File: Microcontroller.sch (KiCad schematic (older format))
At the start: 42 parts, among them CN1 2x10_Way_2.54mm_Pitch_Header, CN2 CONN_RCPT_USB2.0_MINI_B_SMD_R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, J3 DB1C-A1LD, J4 DB1C-A1LD, J5 DB1C-A1LD, U2 STM32L412R8T6, X1 ABM3B-16.000MHZ

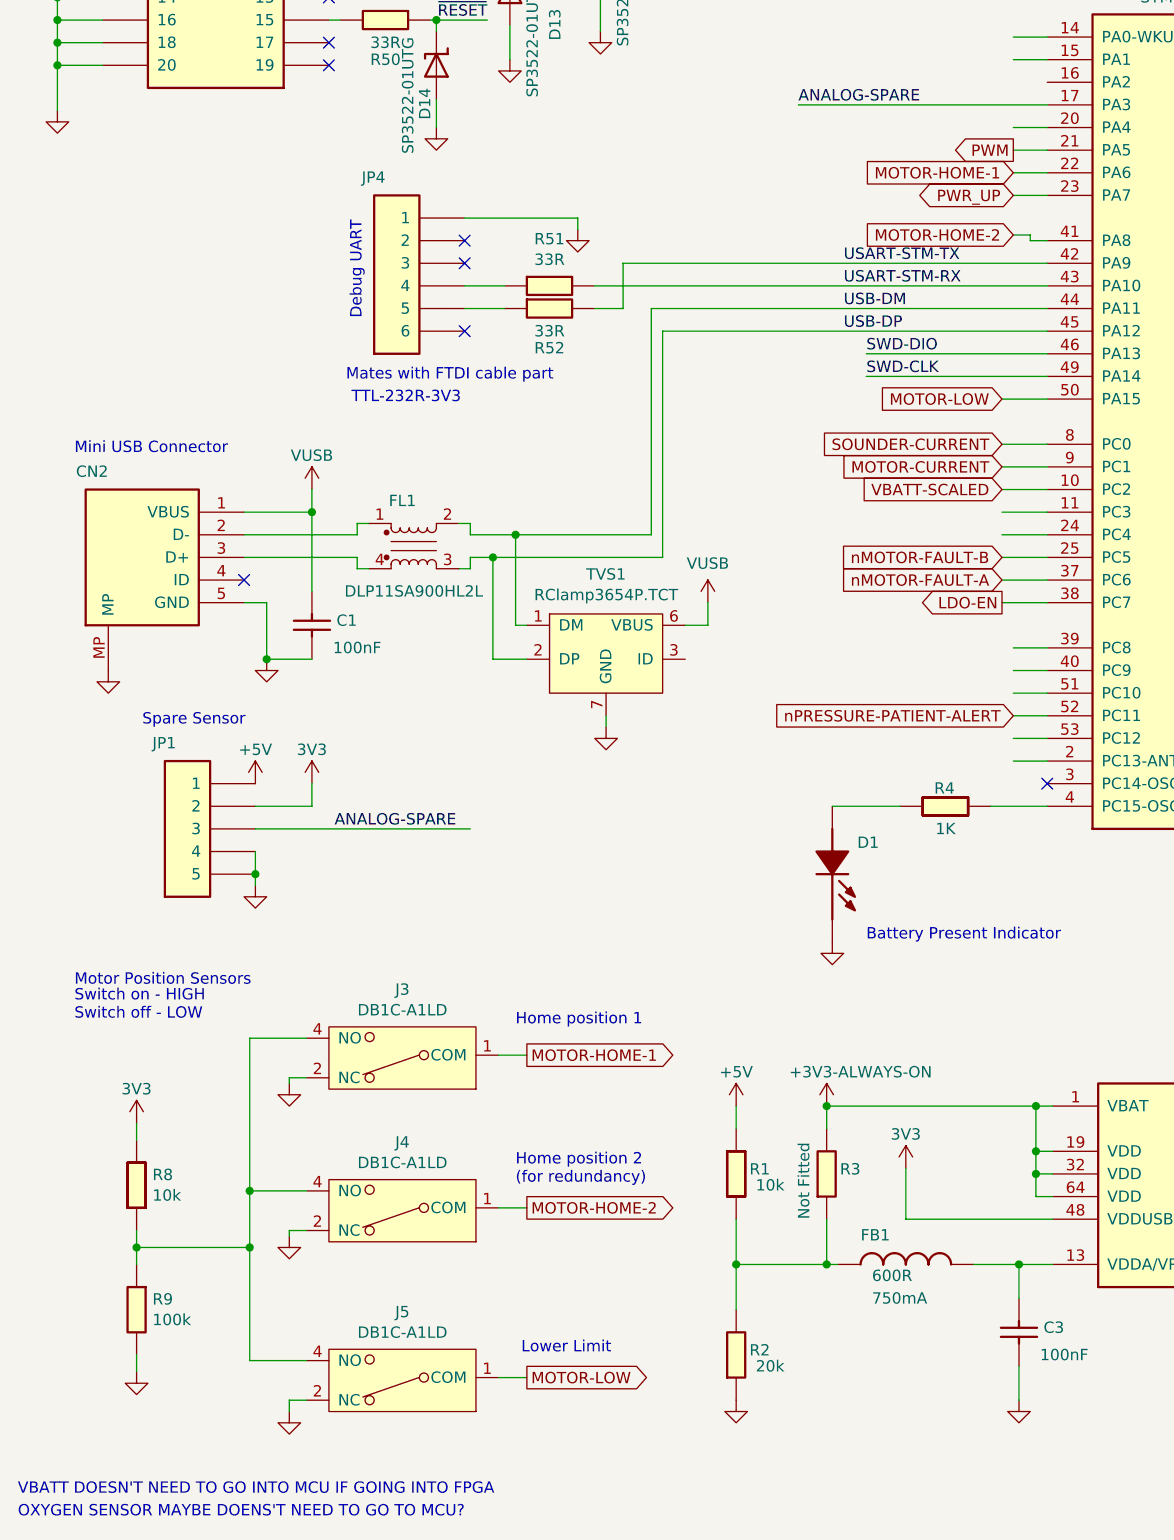
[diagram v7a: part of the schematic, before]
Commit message: On-board Microswitch signals removed from. Microswitch signals from power board renamed to "SW_Home" etc
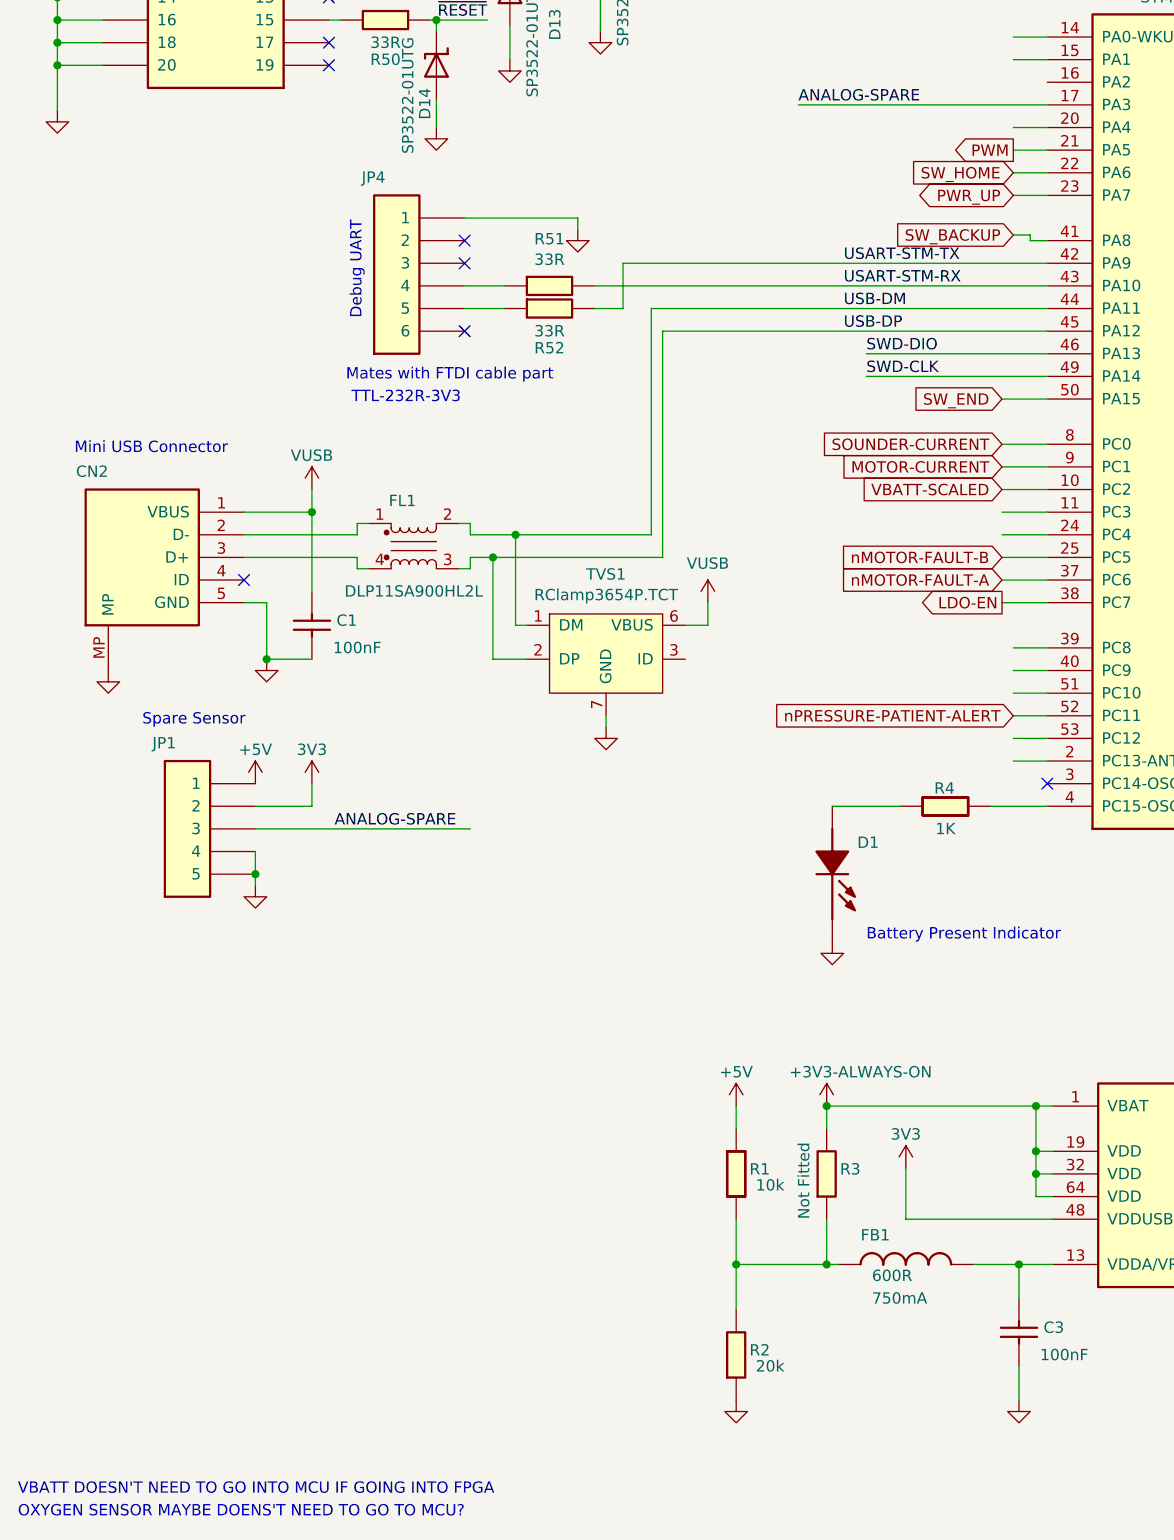
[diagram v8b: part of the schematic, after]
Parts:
- removed J3, J4, J5: DB1C-A1LD, symbol OpenVent-rescue:DB1C-A1LD-OpenVent
- removed R8: 10k_0603_Chip_Resistor,_1%,_0.1W, symbol OpenVent:10k_0603_Chip_Resistor,_1%,_0.1W
- removed R9: 100K_0603_Chip_Resistor,_1%,_0.1W, symbol OpenVent:100K_0603_Chip_Resistor,_1%,_0.1W
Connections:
- net labels added: SW_BACKUP, SW_END, SW_HOME
- net labels removed: MOTOR-HOME-1, MOTOR-HOME-2, MOTOR-LOW
- wire segments 205 -> 185
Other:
- note removed: "Home position 1"
- note removed: "Home position 2\n(for redundancy)"
- note removed: "Lower Limit"
- note removed: "Motor Position Sensors"
- note removed: "Switch on - HIGH\nSwitch off - LOW"
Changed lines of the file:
@@
 Text GLabel 4750 3900 0    50   Input ~ 0
 nMOTOR-FAULT-B
-Text Notes 650  5800 0    50   ~ 0
-Motor Position Sensors
 Text GLabel 4750 4100 0    50   Output ~ 0
 LDO-EN
@@
 Text Notes 400  8150 0    50   ~ 0
 OXYGEN SENSOR MAYBE DOENS'T NEED TO GO TO MCU?
-$Comp
-L OpenVent-rescue:DB1C-A1LD-OpenVent J?
-U 1 1 600C7AA1
-P 2100 6250
-AR Path="/600C7AA1" Ref="J?"  Part="1"
-AR Path="/5F988182/600C7AA1" Ref="J3"  Part="1"
-F 0 "J3" H 2100 5810 50  0000 C CNN
-F 1 "DB1C-A1LD" H 2100 5901 50  0000 C CNN
-F 2 "" H 2100 6250 50  0001 C CNN
-F 3 "" H 2100 6250 50  0001 C CNN
-	1    2100 6250
-	-1   0    0    1
-$EndComp
-$Comp
-L OpenVent-rescue:DB1C-A1LD-OpenVent J?
-U 1 1 600E07E5
-P 2100 6925
-AR Path="/600E07E5" Ref="J?"  Part="1"
-AR Path="/5F988182/600E07E5" Ref="J4"  Part="1"
-F 0 "J4" H 2100 6485 50  0000 C CNN
-F 1 "DB1C-A1LD" H 2100 6576 50  0000 C CNN
-F 2 "" H 2100 6925 50  0001 C CNN
-F 3 "" H 2100 6925 50  0001 C CNN
-	1    2100 6925
-	-1   0    0    1
-$EndComp
-$Comp
-L OpenVent-rescue:DB1C-A1LD-OpenVent J?
-U 1 1 600E171A
-P 2100 7675
-AR Path="/600E171A" Ref="J?"  Part="1"
-AR Path="/5F988182/600E171A" Ref="J5"  Part="1"
-F 0 "J5" H 2100 7235 50  0000 C CNN
-F 1 "DB1C-A1LD" H 2100 7326 50  0000 C CNN
-F 2 "" H 2100 7675 50  0001 C CNN
-F 3 "" H 2100 7675 50  0001 C CNN
-	1    2100 7675
-	-1   0    0    1
-$EndComp
-Text Notes 2600 5975 0    50   ~ 0
-Home position 1
-Text Notes 2600 6675 0    50   ~ 0
-Home position 2\n(for redundancy)
-Text Notes 2625 7425 0    50   ~ 0
-Lower Limit
-Text GLabel 2650 6100 2    50   Output ~ 0
-MOTOR-HOME-1
-Text GLabel 2650 6775 2    50   Output ~ 0
-MOTOR-HOME-2
-Text GLabel 2650 7525 2    50   Output ~ 0
-MOTOR-LOW
-Wire Wire Line
-	2525 6100 2650 6100
-Wire Wire Line
-	2525 6775 2650 6775
-Wire Wire Line
-	2525 7525 2650 7525
-$Comp
-L OpenVent:3V3 #3V3_02
-U 1 1 6025C37A
-P 925 6400
-F 0 "#3V3_02" H 925 6400 20  0001 C CNN
-F 1 "3V3" H 925 6550 50  0000 C CNN
-F 2 "" H 925 6400 70  0001 C CNN
-F 3 "" H 925 6400 70  0001 C CNN
-	1    925  6400
-	1    0    0    -1
-$EndComp
-Text GLabel 4800 2200 0    50   Input ~ 0
-MOTOR-HOME-1
 Text GLabel 4800 2475 0    50   Input ~ 0
-MOTOR-HOME-2
+SW_BACKUP
 Text GLabel 4750 3200 0    50   Input ~ 0
-MOTOR-LOW
+SW_END
 Wire Wire Line
 	4950 3200 4750 3200
@@
 Wire Wire Line
 	4875 2475 4800 2475
-$Comp
-L OpenVent:GND #PWR038
-U 1 1 606DA94E
-P 1600 6225
-F 0 "#PWR038" H 1600 5975 50  0001 C CNN
-F 1 "GND" H 1600 6075 50  0001 C CNN
-F 2 "" H 1600 6225 50  0001 C CNN
-F 3 "" H 1600 6225 50  0001 C CNN
-	1    1600 6225
-	1    0    0    -1
-$EndComp
-$Comp
-L OpenVent:GND #PWR0120
-U 1 1 606DB70A
-P 1600 6900
-F 0 "#PWR0120" H 1600 6650 50  0001 C CNN
-F 1 "GND" H 1600 6750 50  0001 C CNN
-F 2 "" H 1600 6900 50  0001 C CNN
-F 3 "" H 1600 6900 50  0001 C CNN
-	1    1600 6900
-	1    0    0    -1
-$EndComp
-$Comp
-L OpenVent:GND #PWR0121
-U 1 1 606DC2B3
-P 1600 7675
-F 0 "#PWR0121" H 1600 7425 50  0001 C CNN
-F 1 "GND" H 1600 7525 50  0001 C CNN
-F 2 "" H 1600 7675 50  0001 C CNN
-F 3 "" H 1600 7675 50  0001 C CNN
-	1    1600 7675
-	1    0    0    -1
-$EndComp
-Wire Wire Line
-	1675 6200 1600 6200
-Wire Wire Line
-	1600 6200 1600 6225
-Wire Wire Line
-	1675 6875 1600 6875
-Wire Wire Line
-	1600 6875 1600 6900
-Wire Wire Line
-	1675 7625 1600 7625
-Wire Wire Line
-	1600 7625 1600 7675
-$Comp
-L OpenVent:100K_0603_Chip_Resistor,_1%,_0.1W R9
-U 1 1 60814D6B
-P 1025 7125
-F 0 "R9" V 1079 7095 50  0000 L CNN
-F 1 "100K_0603_Chip_Resistor,_1%,_0.1W" H 1025 7125 50  0001 C CNN
-F 2 "" H 1025 7125 50  0001 C CNN
-F 3 "" H 1025 7125 50  0001 C CNN
-F 4 "100k" V 1170 7095 50  0000 L CNN "Val"
-F 5 "1%" H 1025 7125 50  0001 C CNN "Tolerance"
-F 6 "0.1W" H 1025 7125 50  0001 C CNN "Watt"
-	1    1025 7125
-	0    1    1    0
-$EndComp
-$Comp
-L OpenVent:10k_0603_Chip_Resistor,_1%,_0.1W R8
-U 1 1 60815A9F
-P 1025 6575
-F 0 "R8" V 1079 6545 50  0000 L CNN
-F 1 "10k_0603_Chip_Resistor,_1%,_0.1W" H 1025 6575 50  0001 C CNN
-F 2 "" H 1025 6575 50  0001 C CNN
-F 3 "" H 1025 6575 50  0001 C CNN
-F 4 "10k" V 1170 6545 50  0000 L CNN "Val"
-F 5 "1%" H 1025 6575 50  0001 C CNN "Tolerance"
-F 6 "0.1W" H 1025 6575 50  0001 C CNN "Watt"
-	1    1025 6575
-	0    1    1    0
-$EndComp
-$Comp
-L OpenVent:GND #PWR037
-U 1 1 609D1F56
-P 925 7500
-F 0 "#PWR037" H 925 7250 50  0001 C CNN
-F 1 "GND" H 925 7350 50  0001 C CNN
-F 2 "" H 925 7500 50  0001 C CNN
-F 3 "" H 925 7500 50  0001 C CNN
-	1    925  7500
-	1    0    0    -1
-$EndComp
-Wire Wire Line
-	925  7425 925  7500
-Wire Wire Line
-	1675 7450 1425 7450
-Wire Wire Line
-	1425 7450 1425 6950
-Wire Wire Line
-	1425 6950 925  6950
-Wire Wire Line
-	925  6875 925  6950
-Connection ~ 925  6950
-Wire Wire Line
-	925  6950 925  7025
-Wire Wire Line
-	1675 6700 1425 6700
-Connection ~ 1425 6700
-Wire Wire Line
-	1425 6025 1675 6025
-Wire Wire Line
-	925  6475 925  6400
-Text Notes 650  5950 0    50   ~ 0
-Switch on - HIGH\nSwitch off - LOW
-Connection ~ 1425 6950
-Wire Wire Line
-	1425 6950 1425 6700
-Wire Wire Line
-	1425 6025 1425 6700
 Text Label 3250 1125 2    50   ~ 0
 SWD-DIO
@@
 Text Notes 7350 1500 2    50   ~ 0
 SPI1 from MCU to FPGA
+Text GLabel 4800 2200 0    50   Input ~ 0
+SW_HOME
 $EndSCHEMATC
